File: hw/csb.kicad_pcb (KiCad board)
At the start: 2 copper layers, 100 x 90 mm, 60 parts, among them J101 AMPSEAL_23_POS_VERT_BLUE_SEAL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, J102 AMPSEAL_8_POS_VERT_BLACK_SEAL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, J201 ARM_JTAG_SWD_HEADER_10_PINSMD, U1001 ZXCT1086, U1101 ZXCT1086, U1201 ZXCT1086, U201 LPC1549JBD64, U202 MCP2551_SOIC8, U401 MOSFET_DRIVER_LT1161, U402 MOSFET_IPG20N04S4L11ATMA1, U403 MOSFET_IPG20N04S4L11ATMA1, U501 ZXCT1086, U601 ZXCT1086, U701 ZXCT1086, U801 ZXCT1086, U901 MOSFET_DRIVER_LT1161, U902 MOSFET_IPG20N04S4L11ATMA1, U903 MOSFET_IPG20N04S4L11ATMA1, U904 MOSFET_IPG20N04S4L11ATMA1, X201 XTAL_7A-12.000MAAJ-T

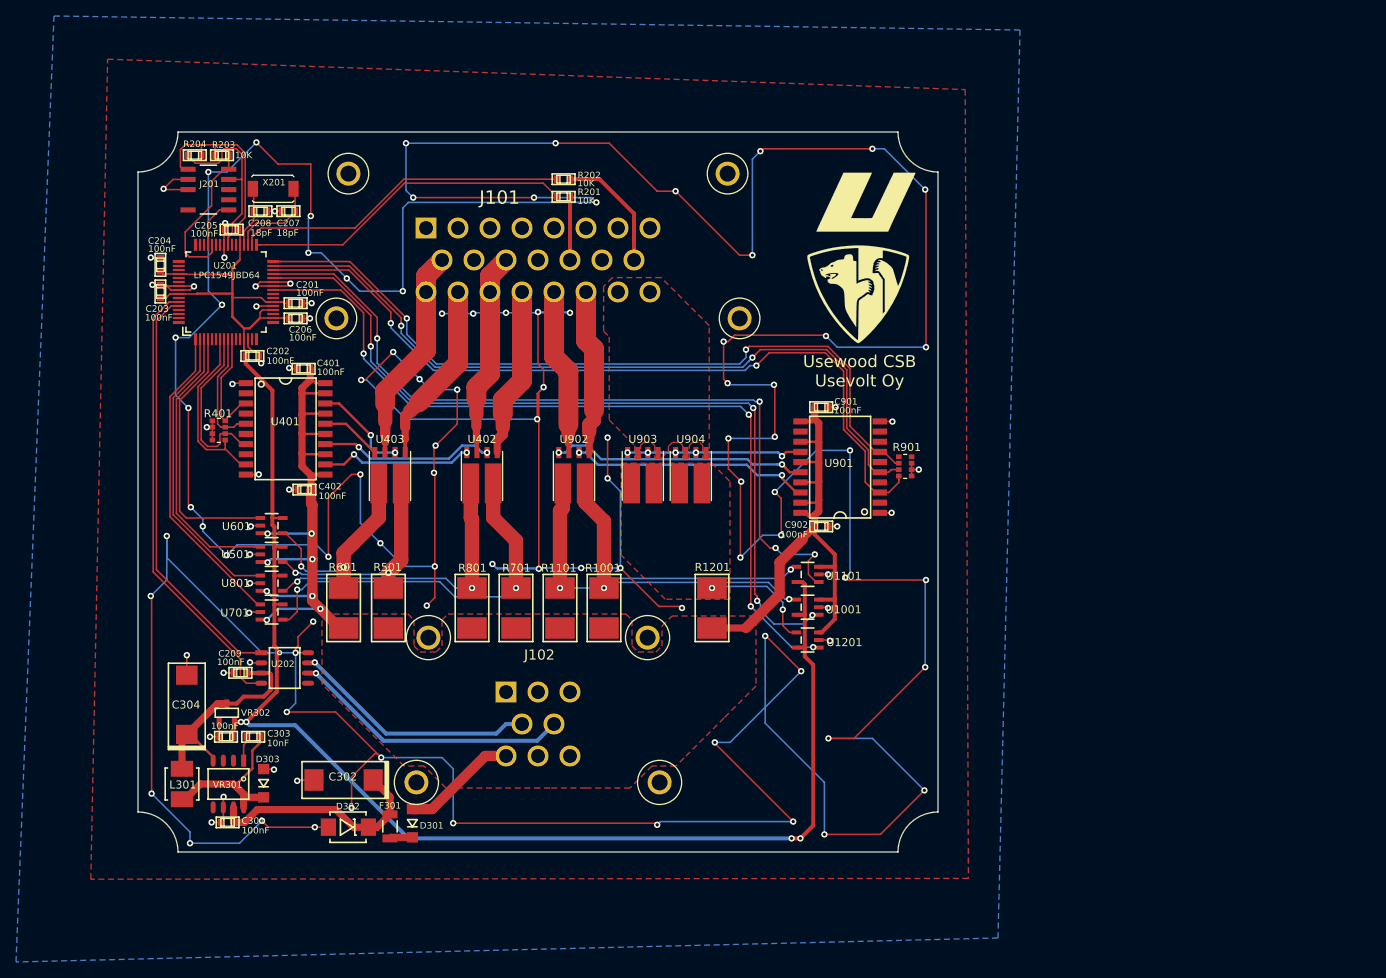
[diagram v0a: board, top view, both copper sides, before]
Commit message: sw directory created, oil cooler added in hw
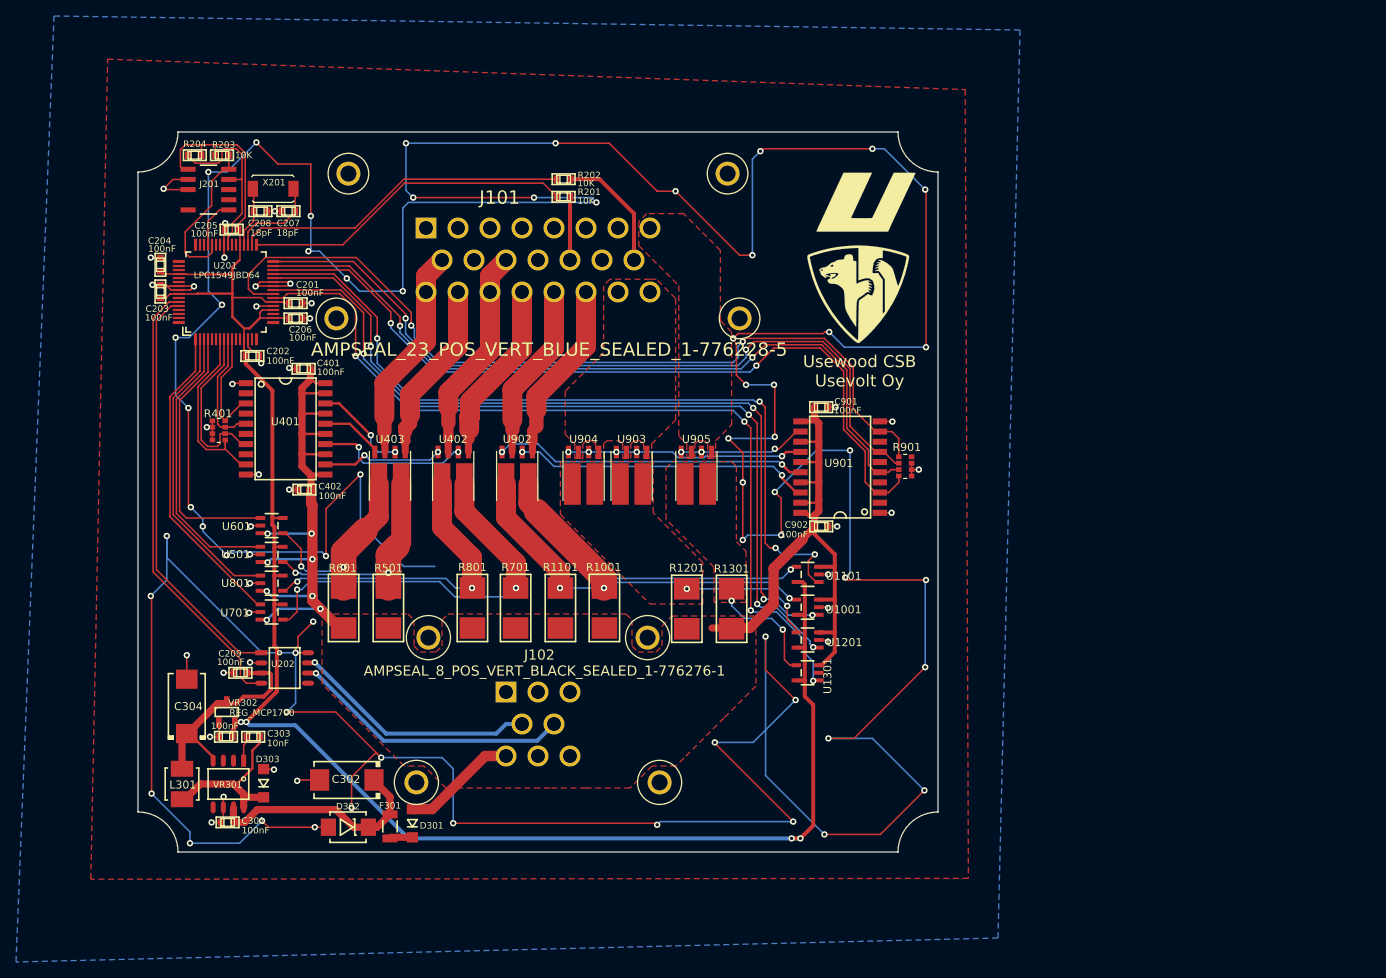
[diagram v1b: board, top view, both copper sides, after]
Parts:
- added R1301: LRMAT2512-R002FT4, usevolt:2512, F.Cu at (192.2, 108.6)
- added U1301: ZXCT1086, usevolt:SOT-25, F.Cu at (201.7, 116.6)
- added U905: MOSFET_IPG20N04S4L11ATMA1, usevolt:PG-TDSON-8-4, F.Cu at (187.8, 92.0)
- moved U904 13.4 mm to (173.7, 92.0)
- moved U902 7.10 mm to (165.4, 92.0)
- moved U402 3.60 mm to (157.4, 92.0)
- moved R1201 3.15 mm to (186.6, 108.6)
- moved U903 1.40 mm to (179.7, 92.0)
- moved C302 0.40 mm to (144.1, 130.0)
- moved C304 0.20 mm to (124.1, 120.8)
- moved VR302 0.10 mm to (129.1, 121.5)
- moved R1001 0.05 mm to (176.3, 108.5)
- moved R1101 0.05 mm to (170.8, 108.5)
- moved R701 0.05 mm to (165.2, 108.5)
- moved R801 0.05 mm to (159.8, 108.5)
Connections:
- J101 pad P$8: (no net) -> /OILCOOLER_15A
- R901 pad 7: (no net) -> /OILCOOLER
- R901 pad 8: (no net) -> GND
- U201 pad P$23: (no net) -> /OILCOOLER_SENSE
- U201 pad P$24: (no net) -> /OILCOOLER
- U901 pad 12: (no net) -> Net-(U901-Pad12)
- U901 pad 9: (no net) -> /OILCOOLER
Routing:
- net GND: track 980.2 -> 799.2 mm, vias 120 -> 97
- net /OILCOOLER_SENSE: track 0.00 -> 107.6 mm, vias 0 -> 4
- net /OILCOOLER: track 0.00 -> 107.0 mm, vias 0 -> 2
- net Net-(U901-Pad12): track 0.00 -> 16.0 mm, vias 0 -> 3
- net /LT1161_2/Sheet59847684/SENSE-: track 0.00 -> 15.4 mm, vias 0 -> 2
- net Net-(U901-Pad14): track 22.0 -> 29.6 mm
- net Net-(U901-Pad16): track 32.0 -> 39.2 mm
- net Net-(U901-Pad18): track 30.0 -> 37.1 mm
- net VDD: track 166.7 -> 173.4 mm
- net Net-(U401-Pad12): track 19.1 -> 15.2 mm
- net Net-(U401-Pad14): track 22.0 -> 19.0 mm
- net /LT1161_2/sheet58BE8E45/SENSE-: track 39.3 -> 42.2 mm
- net /LT1161_2/sheet58BE8E46/SENSE-: track 43.9 -> 46.4 mm
- net /LT1161_2/sheet58BE8E47/SENSE-: track 14.7 -> 17.2 mm
- net /BACK_2A: track 21.4 -> 23.6 mm
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- added copper zone on F.Cu, net /LT1161_2/Sheet59847684/SENSE-
- added copper zone on F.Cu, net /OILCOOLER_15A

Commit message: revision 2.0.0 pcb ready to order
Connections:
- R401 pad 1: /DRIVE -> /BEACON
- R401 pad 3: /BEACON -> /DRIVE
- R401 pad 5: /WORK -> /BACK
- R401 pad 7: /BACK -> /WORK
- R901 pad 1: /IN -> /WIPER
- R901 pad 3: /WIPER -> /IN
- U1001 pad 1: /IN_SENSE -> /WIPER_SENSE
- U1101 pad 1: /WIPER_SENSE -> /IN_SENSE
- U201 pad P$1: /WORK_SENSE -> /BACK_SENSE
- U201 pad P$10: /DRIVE -> /BEACON
- U201 pad P$2: /BACK_SENSE -> /WORK_SENSE
- U201 pad P$28: /IN_SENSE -> /WIPER_SENSE
- U201 pad P$29: /WIPER_SENSE -> /IN_SENSE
- U201 pad P$3: /DRIVE_SENSE -> /BEACON_SENSE
- U201 pad P$30: /IN -> /WIPER
- U201 pad P$31: /WIPER -> /IN
- U201 pad P$4: /BEACON_SENSE -> /DRIVE_SENSE
- U201 pad P$7: /BACK -> /WORK
- U201 pad P$8: /WORK -> /BACK
- U201 pad P$9: /BEACON -> /DRIVE
- U401 pad 3: /DRIVE -> /BEACON
- U401 pad 5: /BEACON -> /DRIVE
- U401 pad 7: /WORK -> /BACK
- U401 pad 9: /BACK -> /WORK
- U501 pad 1: /DRIVE_SENSE -> /BEACON_SENSE
- U601 pad 1: /BEACON_SENSE -> /DRIVE_SENSE
- U701 pad 1: /WORK_SENSE -> /BACK_SENSE
- U801 pad 1: /BACK_SENSE -> /WORK_SENSE
- U901 pad 3: /IN -> /WIPER
- U901 pad 5: /WIPER -> /IN
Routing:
- net GND: track 799.2 -> 903.5 mm, vias 97 -> 110
- net /WIPER: track 98.0 -> 101.2 mm
- net /IN: track 101.2 -> 98.0 mm
- net /WIPER_SENSE: track 100.1 -> 102.3 mm
- net /IN_SENSE: track 102.3 -> 100.1 mm
- net /DRIVE_SENSE: track 35.4 -> 33.4 mm
- net /BEACON_SENSE: track 33.4 -> 35.4 mm
- net /WORK_SENSE: track 39.4 -> 37.4 mm
- net /BACK_SENSE: track 37.4 -> 39.4 mm
- net /WORK: track 21.6 -> 22.3 mm
- net /BACK: track 22.3 -> 21.6 mm
- net /DRIVE: track 14.5 -> 15.0 mm
- net /BEACON: track 15.0 -> 14.5 mm

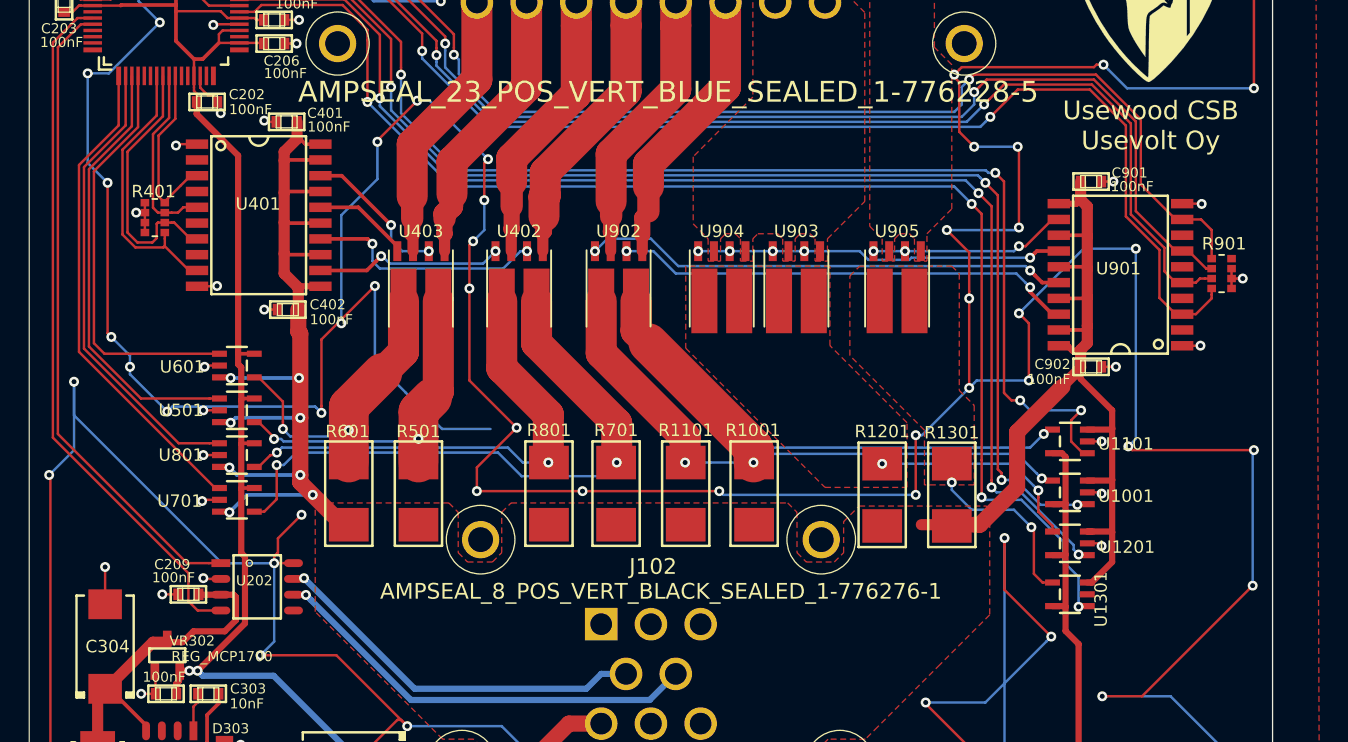
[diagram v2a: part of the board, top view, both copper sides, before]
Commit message: at least shortcirucuit protection works
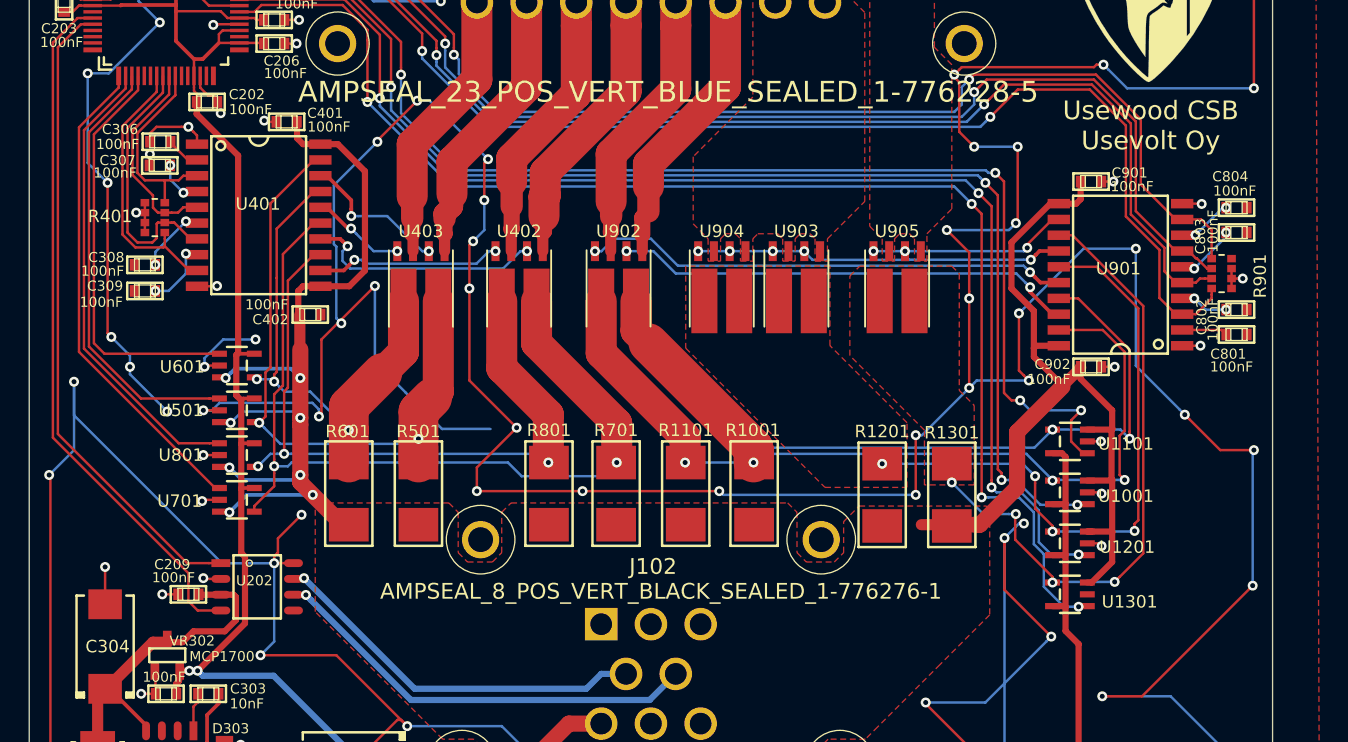
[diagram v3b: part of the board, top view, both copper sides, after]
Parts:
- added C306: 100nF, kemet:0603, F.Cu at (128.5, 80.2)
- added C307: 100nF, kemet:0603, F.Cu at (128.5, 82.1)
- added C308: 100nF, kemet:0603, F.Cu at (127.3, 90.1)
- added C309: 100nF, kemet:0603, F.Cu at (127.3, 92.2)
- added C801: 100nF, kemet:0603, F.Cu at (215.1, 95.7)
- added C802: 100nF, kemet:0603, F.Cu at (215.1, 93.7)
- added C803: 100nF, kemet:0603, F.Cu at (215.1, 87.5)
- added C804: 100nF, kemet:0603, F.Cu at (215.1, 85.5)
- VR302: value REG_MCP1700 -> MCP1700
- moved C402 1.84 mm to (140.6, 94.1), turned to 0 degrees
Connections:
- U401 pad 13: VDD -> /LT1161/sheet58BE8E48/SENSE-
- U401 pad 15: VDD -> /LT1161/sheet58BE8E47/SENSE-
- U401 pad 17: VDD -> /LT1161/sheet58BE8E46/SENSE-
- U401 pad 19: VDD -> /LT1161/sheet58BE8E45/SENSE-
- U401 pad 2: (no net) -> Net-(C306-Pad2)
- U401 pad 4: (no net) -> Net-(C307-Pad2)
- U401 pad 6: (no net) -> Net-(C308-Pad2)
- U401 pad 8: (no net) -> Net-(C309-Pad2)
- U901 pad 13: VDD -> /LT1161_2/Sheet59847684/SENSE-
- U901 pad 15: VDD -> /LT1161_2/sheet58BE8E47/SENSE-
- U901 pad 17: VDD -> /LT1161_2/sheet58BE8E46/SENSE-
- U901 pad 19: VDD -> /LT1161_2/sheet58BE8E45/SENSE-
- U901 pad 2: (no net) -> Net-(C801-Pad2)
- U901 pad 4: (no net) -> Net-(C802-Pad2)
- U901 pad 6: (no net) -> Net-(C803-Pad2)
- U901 pad 8: (no net) -> Net-(C804-Pad2)
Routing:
- net /LT1161_2/Sheet59847684/SENSE-: track 15.4 -> 51.8 mm, vias 2 -> 4
- net /LT1161_2/sheet58BE8E47/SENSE-: track 17.2 -> 50.2 mm, vias 2 -> 4
- net /LT1161/sheet58BE8E45/SENSE-: track 27.7 -> 51.2 mm
- net /LT1161_2/sheet58BE8E45/SENSE-: track 42.2 -> 64.7 mm, vias 2 -> 3
- net /LT1161_2/sheet58BE8E46/SENSE-: track 46.4 -> 67.9 mm, vias 2 -> 3
- net /LT1161/sheet58BE8E47/SENSE-: track 49.7 -> 70.3 mm
- net /LT1161/sheet58BE8E48/SENSE-: track 39.5 -> 56.5 mm, vias 2 -> 3
- net /LT1161/sheet58BE8E46/SENSE-: track 25.9 -> 41.3 mm, vias 2 -> 3
- net VDD: track 173.4 -> 161.4 mm
- net Net-(C309-Pad2): track 0.00 -> 5.57 mm, vias 0 -> 2
- net Net-(C308-Pad2): track 0.00 -> 5.47 mm, vias 0 -> 2
- net Net-(C803-Pad2): track 0.00 -> 4.99 mm, vias 0 -> 2
- net GND: track 903.5 -> 908.1 mm, vias 110 -> 112
- net Net-(C804-Pad2): track 0.00 -> 4.45 mm, vias 0 -> 2
- net Net-(C802-Pad2): track 0.00 -> 3.91 mm, vias 0 -> 2
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
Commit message: starting to draw version 4.0.0
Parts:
- removed C206, C209, C307, C308, C309, C401, C402, C901, C902: 100nF, kemet:0603
- removed C207, C208: 18pF, kemet:0603
- removed D301, D303: DIODE_RS07J-GS18, usevolt:DO219AB
- removed D302: DIODE_TVS_SMBJ33A-TRDO-214AA, usevolt:DO-214AA
- removed F301: FUSE_MC36211_350MA, usevolt:FUSE_MC36211
- removed J201: ARM_JTAG_SWD_HEADER_10_PINSMD, usevolt:ARM_10_PIN_JTAG_SWD_CONNECTOR
- removed L301: IND_744045210, usevolt:IND_744045210
- removed R201, R202, R203, R204: 10K, multicomp:0603
- removed U201: LPC1549JBD64, usevolt:QFP64
- removed U202: MCP2551_SOIC8, usevolt:SOIC8
- removed U402, U403, U902, U903, U904, U905: MOSFET_IPG20N04S4L11ATMA1, usevolt:PG-TDSON-8-4
- removed VR301: LM2671SOIC8, usevolt:SOIC8
- removed VR302: MCP1700, usevolt:SOT-23_3-PIN
- removed X201: XTAL_7A-12.000MAAJ-T, usevolt:XTAL_7A-20.000MAJ
- added C1301: 100nF, kemet:0603, F.Cu at (264.3, 108.5)
- added C1302: 100nF, kemet:0603, F.Cu at (253.9, 109.6)
- added C1303: 100nF, kemet:0603, F.Cu at (258.7, 109.6)
- added C1304: 100nF, kemet:0603, F.Cu at (238.8, 114.2)
- added C1305: 100nF, kemet:0603, F.Cu at (243.6, 110.3)
- added C1306: 100nF, kemet:0603, F.Cu at (269.1, 103.9)
- added C1307: 18pF, kemet:0603, F.Cu at (257.1, 114.2)
- added C1308: 18pF, kemet:0603, F.Cu at (252.5, 114.9)
- added C1309: 100nF, kemet:0603, F.Cu at (264.3, 103.9)
- added C805: 100nF, kemet:0603, F.Cu at (203.4, 83.4)
- added C806: 100nF, kemet:0603, F.Cu at (203.4, 98.3)
- added D201: DIODE_RS07J-GS18, usevolt:DO219AB, F.Cu at (152.4, 135.4)
- added D202: DIODE_TVS_SMBJ33A-TRDO-214AA, usevolt:DO-214AA, F.Cu at (144.3, 135.9)
- added D203: DIODE_RS07J-GS18, usevolt:DO219AB, F.Cu at (133.7, 130.4)
- added F201: FUSE_MC36211_350MA, usevolt:FUSE_MC36211, F.Cu at (149.5, 135.8)
- added J1301: ARM_JTAG_SWD_HEADER_10_PINSMD, usevolt:ARM_10_PIN_JTAG_SWD_CONNECTOR, F.Cu at (126.8, 56.2)
- added L201: IND_744045210, usevolt:IND_744045210, F.Cu at (123.5, 130.5)
- added R1302: 10K, multicomp:0603, F.Cu at (247.9, 114.9)
- added R1303: 10K, multicomp:0603, F.Cu at (243.3, 114.9)
- added R1304: 10K, multicomp:0603, F.Cu at (248.2, 110.3)
- added R301: R_ARRAY4_1K, usevolt:0603_array4, F.Cu at (128.1, 86.3)
- added U1302: MCP2551_SOIC8, usevolt:SOIC8, F.Cu at (136.3, 116.0)
- added U301: MOSFET_DRIVER_LT1161, usevolt:SO20, F.Cu at (136.4, 86.1)
- added U302: MOSFET_IPG20N04S4L11ATMA1, usevolt:PG-TDSON-8-4, F.Cu at (154.9, 92.0)
- added U303: MOSFET_IPG20N04S4L11ATMA1, usevolt:PG-TDSON-8-4, F.Cu at (161.5, 92.0)
- added U304: MOSFET_IPG20N04S4L11ATMA1, usevolt:PG-TDSON-8-4, F.Cu at (148.3, 92.0)
- added U802: MOSFET_IPG20N04S4L11ATMA1, usevolt:PG-TDSON-8-4, F.Cu at (168.1, 92.0)
- added U803: MOSFET_IPG20N04S4L11ATMA1, usevolt:PG-TDSON-8-4, F.Cu at (174.6, 92.0)
- added U804: MOSFET_IPG20N04S4L11ATMA1, usevolt:PG-TDSON-8-4, F.Cu at (181.2, 92.0)
- added U805: MOSFET_IPG20N04S4L11ATMA1, usevolt:PG-TDSON-8-4, F.Cu at (187.8, 92.0)
- added VR201: LM2671SOIC8, usevolt:SOIC8, F.Cu at (129.3, 130.6)
- added VR202: REG_MCP1700, usevolt:SOT-23_3-PIN, F.Cu at (129.1, 121.5)
- added X1301: XTAL_7A-12.000MAAJ-T, usevolt:XTAL_7A-20.000MAJ, F.Cu at (134.9, 56.1)
- C202, C204: value 100nF -> T491D226K035AT; footprint kemet:0603 -> kemet:7343
- C203: value 100nF -> 10nF
- C302, C304: value T491D226K035AT -> 100nF; footprint kemet:7343 -> kemet:0603
- C303: value 10nF -> 100nF
- R1201, R501, R701: value LRMAT2512-R002FT4 -> LRMAT2512-R004FT4
- R1301: value LRMAT2512-R002FT4 -> 10K; footprint usevolt:2512 -> multicomp:0603
- R401: value R_ARRAY4_1K -> LRMAM1206-R015FT5; footprint usevolt:0603_array4 -> usevolt:1206
- R601: value LRMAT2512-R002FT4 -> LRMAM1206-R015FT5; footprint usevolt:2512 -> usevolt:1206
- R801: value LRMAT2512-R002FT4 -> R_ARRAY4_1K; footprint usevolt:2512 -> usevolt:0603_array4
- R901: value R_ARRAY4_1K -> LRMAT2512-R002FT4; footprint usevolt:0603_array4 -> usevolt:2512
- U1301: value ZXCT1086 -> LPC1549JBD64; footprint usevolt:SOT-25 -> usevolt:QFP64
- U401, U901: value MOSFET_DRIVER_LT1161 -> ZXCT1086; footprint usevolt:SO20 -> usevolt:SOT-25
- U801: value ZXCT1086 -> MOSFET_DRIVER_LT1161; footprint usevolt:SOT-25 -> usevolt:SO20
- moved U401 119.7 mm to (256.1, 87.6)
- moved U701 99.1 mm to (232.5, 93.2)
- moved U501 98.2 mm to (232.0, 88.9)
- moved U601 97.0 mm to (230.8, 84.9)
- moved U1301 86.9 mm to (129.0, 69.0), turned to 0 degrees
- moved C201 77.1 mm to (139.0, 147.5)
- moved C203 75.6 mm to (127.5, 144.2)
- moved U801 72.4 mm to (205.7, 90.9)
- moved C205 63.4 mm to (129.0, 124.6)
- moved R1301 61.3 mm to (250.4, 128.0)
- moved R801 56.9 mm to (213.9, 90.8)
- moved C204 55.3 mm to (124.1, 120.8)
- moved C301 55.0 mm to (128.5, 80.3), turned to 0 degrees
- moved C202 54.3 mm to (144.1, 130.0), turned to 180 degrees
- moved C302 50.4 mm to (128.5, 82.1), turned to 0 degrees
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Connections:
- net /DRIVE_5A renamed /DRIVE_15A
- C201 pad 1: +3V3 -> Net-(C201-Pad1)
- C203 pad 1: +3V3 -> Net-(C203-Pad1)
- C203 pad 2: GND -> Net-(C203-Pad2)
- C301 pad 1: Net-(C301-Pad1) -> GND
- C301 pad 2: GND -> Net-(C301-Pad2)
- C303 pad 1: Net-(C303-Pad1) -> GND
- C305 pad 1: +3V3 -> VDD
- C306 pad 1: GND -> VDD
- C306 pad 2: Net-(C306-Pad2) -> GND
- J101 pad P$10: (no net) -> /WORK_15A
- J101 pad P$11: /WORK_5A -> (no net)
- J101 pad P$17: /BEACON_2A -> /WORK_15A
- J101 pad P$18: /WORK_5A -> /BEACON_4A
- J101 pad P$19: /BACK_2A -> /BACK_4A
- J101 pad P$20: /IN_2A -> /IN_4A
- J101 pad P$21: /WIPER_2A -> /WIPER_4A
- R1001 pad 1: /LT1161_2/sheet58BE8E45/SENSE- -> /LT1161_2/sheet58BE8E46/SENSE-
- R1101 pad 1: /LT1161_2/sheet58BE8E46/SENSE- -> /LT1161_2/sheet58BE8E47/SENSE-
- R1201 pad 1: /LT1161_2/sheet58BE8E47/SENSE- -> /LT1161_2/Sheet59847684/SENSE-
- R1301 pad 1: /LT1161_2/Sheet59847684/SENSE- -> /LPC1549/WIPER_POS
- R1301 pad 2: VDD -> Net-(R1301-Pad2)
- R401 pad 1: /BEACON -> /LT1161/sheet58BE8E45/SENSE-
- R401 pad 2: GND -> VDD
- R501 pad 1: /LT1161/sheet58BE8E45/SENSE- -> /LT1161/sheet58BE8E46/SENSE-
- R601 pad 1: /LT1161/sheet58BE8E46/SENSE- -> /LT1161/sheet58BE8E47/SENSE-
- R701 pad 1: /LT1161/sheet58BE8E47/SENSE- -> /LT1161/sheet58BE8E48/SENSE-
- R801 pad 1: /LT1161/sheet58BE8E48/SENSE- -> /WIPER
- R801 pad 2: VDD -> GND
- R901 pad 1: /WIPER -> /LT1161_2/sheet58BE8E45/SENSE-
- R901 pad 2: GND -> VDD
- U1001 pad 1: /WIPER_SENSE -> /IN_SENSE
- U1001 pad 4: /LT1161_2/sheet58BE8E45/SENSE- -> /LT1161_2/sheet58BE8E46/SENSE-
- U1101 pad 1: /IN_SENSE -> /COOLER_SENSE
- U1101 pad 4: /LT1161_2/sheet58BE8E46/SENSE- -> /LT1161_2/sheet58BE8E47/SENSE-
- U1201 pad 1: /COOLER_SENSE -> /OILCOOLER_SENSE
- U1201 pad 4: /LT1161_2/sheet58BE8E47/SENSE- -> /LT1161_2/Sheet59847684/SENSE-
- U401 pad 1: GND -> /BEACON_SENSE
- U401 pad 2: Net-(C306-Pad2) -> GND
- U401 pad 3: /BEACON -> VDD
- U401 pad 4: Net-(C307-Pad2) -> /LT1161/sheet58BE8E45/SENSE-
- U401 pad 5: /DRIVE -> +3V3
- U501 pad 1: /BEACON_SENSE -> /DRIVE_SENSE
- U501 pad 4: /LT1161/sheet58BE8E45/SENSE- -> /LT1161/sheet58BE8E46/SENSE-
- U601 pad 1: /DRIVE_SENSE -> /BACK_SENSE
- U601 pad 4: /LT1161/sheet58BE8E46/SENSE- -> /LT1161/sheet58BE8E47/SENSE-
- U701 pad 1: /BACK_SENSE -> /WORK_SENSE
- U701 pad 4: /LT1161/sheet58BE8E47/SENSE- -> /LT1161/sheet58BE8E48/SENSE-
- U801 pad 1: /WORK_SENSE -> GND
- U801 pad 2: GND -> Net-(C801-Pad2)
- U801 pad 3: VDD -> /WIPER
- U801 pad 4: /LT1161/sheet58BE8E48/SENSE- -> Net-(C802-Pad2)
- U801 pad 5: +3V3 -> /IN
- U901 pad 1: GND -> /WIPER_SENSE
- U901 pad 2: Net-(C801-Pad2) -> GND
- U901 pad 3: /WIPER -> VDD
- U901 pad 4: Net-(C802-Pad2) -> /LT1161_2/sheet58BE8E45/SENSE-
- U901 pad 5: /IN -> +3V3
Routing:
- net (no net): track 0.00 -> 774.6 mm, vias 0 -> 45
- net GND: track 908.1 -> 503.0 mm, vias 112 -> 46
- net /BACK: track 21.6 -> 222.1 mm, vias 0 -> 14
- net VDD: track 161.4 -> 277.0 mm, vias 8 -> 10
- net Net-(C801-Pad2): track 3.68 -> 117.6 mm, vias 0 -> 14
- net /OILCOOLER: track 107.0 -> 0.00 mm, vias 2 -> 0
- net /WIPER_SENSE: track 102.3 -> 0.00 mm, vias 4 -> 0
- net /WIPER: track 101.2 -> 0.00 mm, vias 2 -> 0
- net /IN: track 98.0 -> 0.00 mm, vias 2 -> 0
- net /COOLER: track 97.4 -> 0.00 mm, vias 2 -> 0
- net /LPC1549/CAN_RX: track 56.8 -> 0.00 mm
- net /LT1161/sheet58BE8E47/SENSE-: track 70.3 -> 17.8 mm, vias 2 -> 3
- net /LPC1549/CAN_TX: track 52.1 -> 0.00 mm
- net Net-(R1301-Pad2): track 0.00 -> 51.8 mm, vias 0 -> 4
- net /LT1161_2/sheet58BE8E45/SENSE-: track 64.7 -> 112.0 mm, vias 3 -> 4
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- removed copper zone on F.Cu, net /COOLER_30A
- removed copper zone on F.Cu, net /LT1161_2/sheet58BE8E47/SENSE-
